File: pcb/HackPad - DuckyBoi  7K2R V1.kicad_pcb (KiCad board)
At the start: 2 copper layers, 79.2 x 60.8 mm, 26 parts, among them SW1 RotaryEncoder_Switch, SW2 RotaryEncoder_Switch, SW3 SW_Push, SW4 SW_Push, SW5 SW_Push, SW6 SW_Push, SW7 SW_Push, SW8 SW_Push, SW9 SW_Push, U1 XIAO-RP2040-DIP

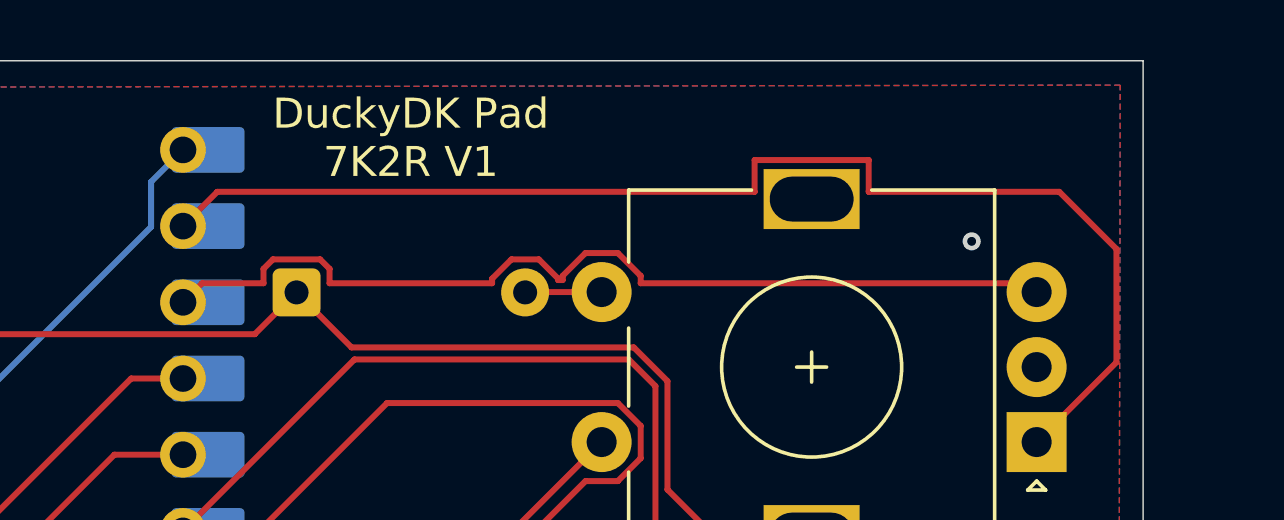
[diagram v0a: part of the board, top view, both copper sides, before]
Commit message: Fixed Sharp corners on pcb
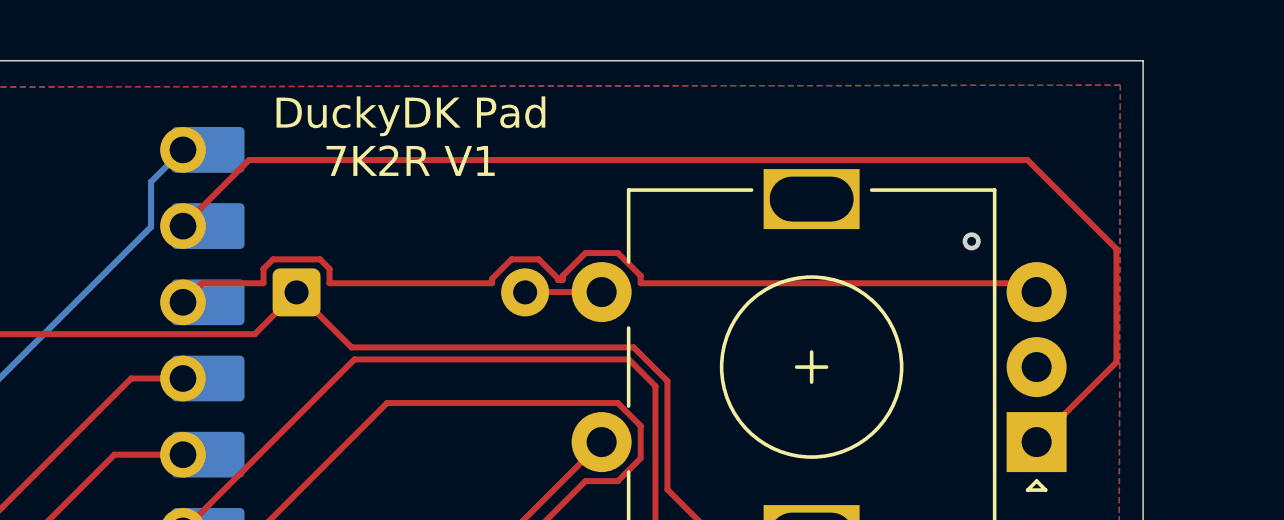
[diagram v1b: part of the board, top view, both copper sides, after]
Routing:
- net ROT2-A: track 42.0 -> 40.8 mm
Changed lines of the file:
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@@
 	)
 	(segment
-		(start 139.958 76.665)
-		(end 139.958 77.724)
-		(width 0.2)
-		(layer "F.Cu")
-		(net 24)
-	)
-	(segment
-		(start 152.019 79.629)
-		(end 150.114 77.724)
-		(width 0.2)
-		(layer "F.Cu")
-		(net 24)
-	)
-	(segment
-		(start 139.958 77.724)
-		(end 122.047 77.724)
-		(width 0.2)
-		(layer "F.Cu")
-		(net 24)
-	)
-	(segment
-		(start 122.047 77.724)
-		(end 120.904 78.867)
-		(width 0.2)
-		(layer "F.Cu")
-		(net 24)
-	)
-	(segment
-		(start 150.114 77.724)
-		(end 143.76 77.724)
-		(width 0.2)
-		(layer "F.Cu")
-		(net 24)
-	)
-	(segment
-		(start 143.76 77.724)
-		(end 143.76 76.665)
-		(width 0.2)
-		(layer "F.Cu")
-		(net 24)
-	)
-	(segment
-		(start 143.76 76.665)
-		(end 139.958 76.665)
+		(start 152.019 83.406)
+		(end 152.019 79.629)
 		(width 0.2)
 		(layer "F.Cu")
@@
 	)
 	(segment
-		(start 152.019 83.406)
-		(end 152.019 79.629)
+		(start 152.019 79.629)
+		(end 149.055 76.665)
 		(width 0.2)
 		(layer "F.Cu")
+		(net 24)
+	)
+	(segment
+		(start 149.055 76.665)
+		(end 123.106 76.665)
+		(width 0.2)
+		(layer "F.Cu")
+		(net 24)
+	)
+	(segment
+		(start 123.106 76.665)
+		(end 120.904 78.867)
+		(width 0.2)
+		(layer "F.Cu")
